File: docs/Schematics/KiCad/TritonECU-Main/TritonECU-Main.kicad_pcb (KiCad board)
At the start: 4 copper layers, 158 x 174 mm, 4 parts, among them J1 EEC-V 104

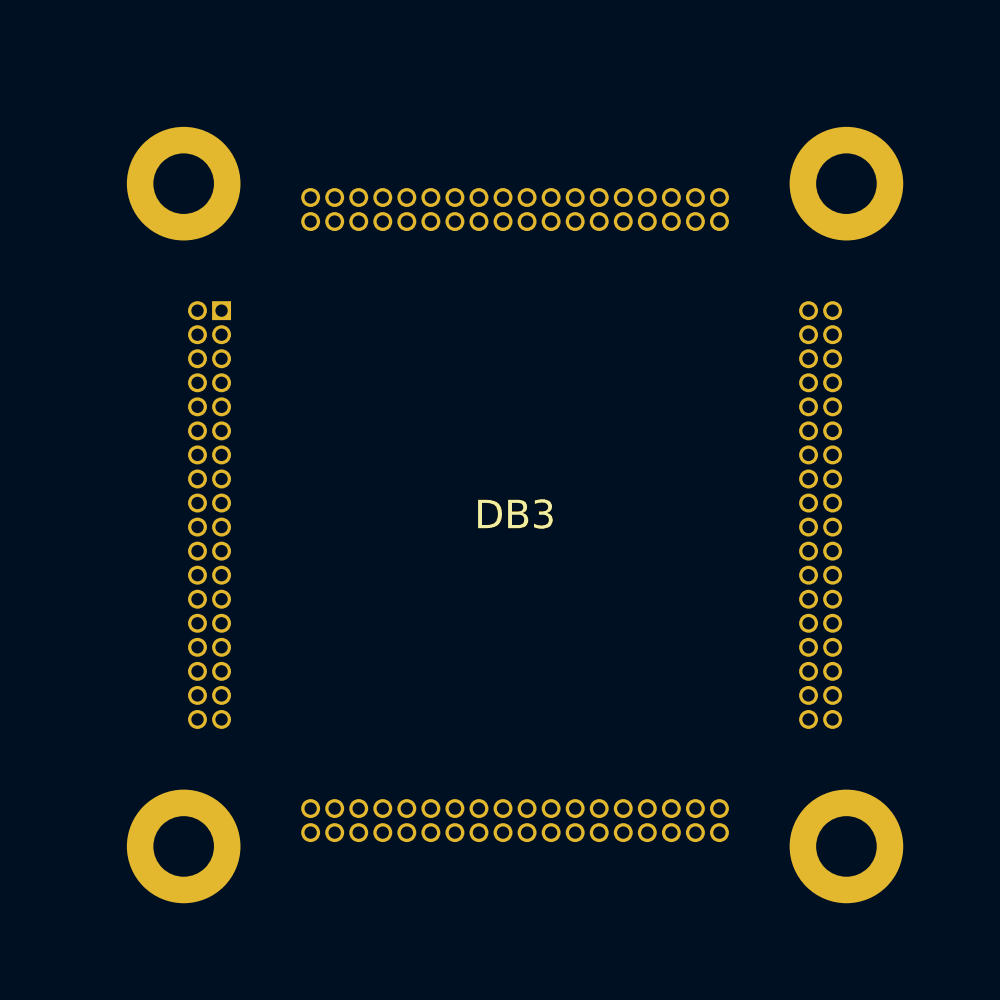
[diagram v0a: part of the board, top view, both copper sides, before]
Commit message: MCU module: place 6-layer PCB with Samtec SMT headers and STDC14
gen_module_pcb.py builds the 44 x 44 mm, 6-layer module board in KiCad's
Python. The stack is F sig / In1 GND / In2 sig / In3 sig / In4 +3.3V / B sig.
The F767 is on top; decoupling, crystals and the headers are on the bottom.

The headers are Samtec TFM-118-22-L-D-A (module bottom) and
SFM-118-02-S-D-A-N-K-TR (carrier top), both SMT. Pad geometry and alignment
holes come from the vendor footprints imported via Component Search Engine;
positions come from mcu_pinout.py, and the rows now sit at 16.5 mm so the TFM
bodies clear at the corners. The carrier DB3 footprint is regenerated to match,
and all 144 pins are verified to mate.

The H1 standoff is offset 0.7 mm per axis, so the module fits only one way
round: the no-notch socket and four identical headers give no polarization.

An STDC14 programming header (FTSH-107, SMT) on the module top carries SWD,
SWO, NRST and the ST-Link VCP on USART3 PD8/PD9. Passives use hand-solder
footprints.

Co-Authored-By: Claude Opus 5.5 <noreply@anthropic.com>
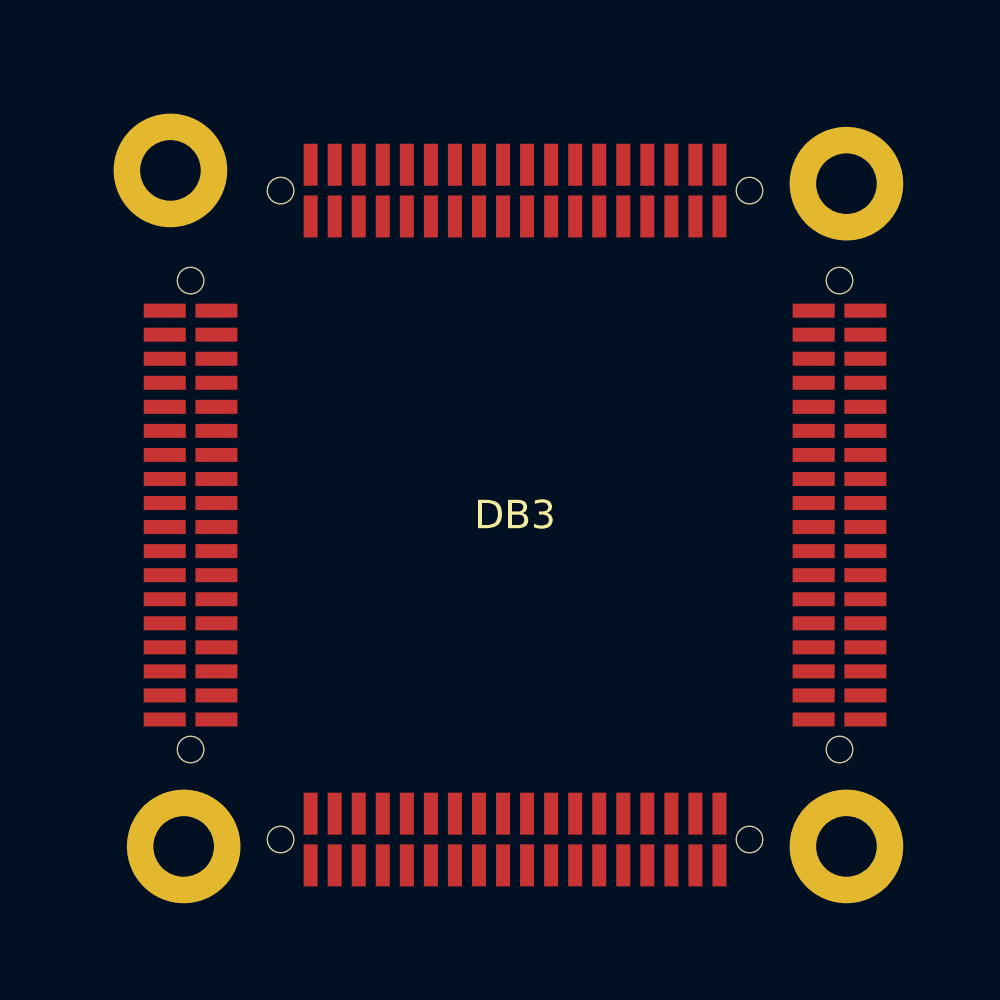
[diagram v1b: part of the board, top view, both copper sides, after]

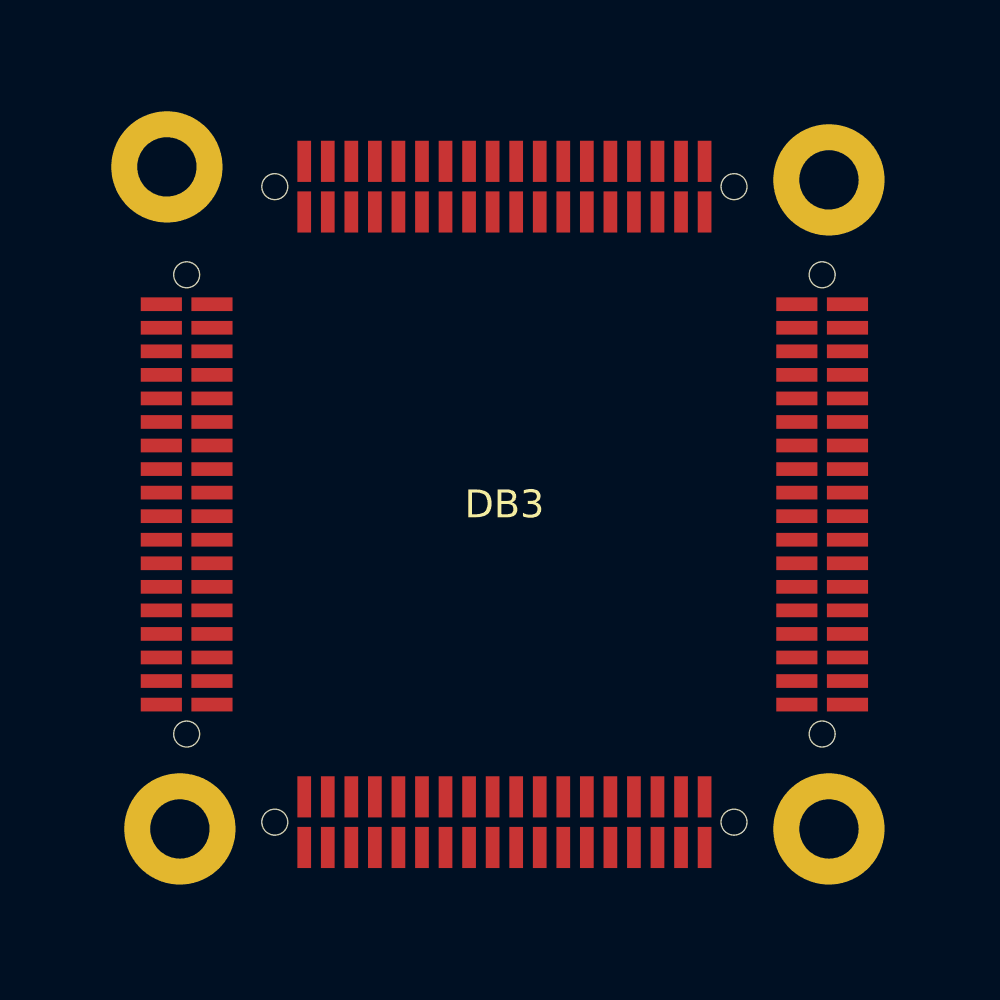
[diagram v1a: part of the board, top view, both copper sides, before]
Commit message: MCU module: route 46 mm board on Samtec FTSH/FLE with Wurth/PEM standoffs
- Interconnect: FTSH-118-02-L-DV-A (module bottom) mating FLE-118-01-G-DV-K-TR
  (carrier top), 7.47 mm stack, replacing TFM-118-22 / SFM-118-02. FTSH pads
  trimmed 0.1 mm at the inner end for the 0.25 mm hole clearance to the -A
  alignment holes.
- Standoffs: Wurth 9774050982R 5 mm SMT spacer on the module, PEM
  SMTSO-M3-2ET 2 mm on the carrier, 0.5 mm M3 washer between (7.5 mm),
  M3 x 10 screw. Spacer footprint generated from the Wurth land pattern with
  a GND ring, plus Wurth's STEP model.
- Module grows 44 -> 46 mm for the spacer pads; H1 keying offset now inward.
- Board routed with Freerouting: DRC 0 violations, 0 unconnected, schematic
  parity clean. All parts included in the BOM; supplier BOM exports added.
- Generators: fix footprint-to-symbol links (netlist tstamps regex), copy all
  schematic fields, skip no-connect pins, footprint-only mode in gen_module.py,
  carrier floor plan refreshes a changed mate footprint in place.

Co-Authored-By: Claude Opus 5.5 <noreply@anthropic.com>
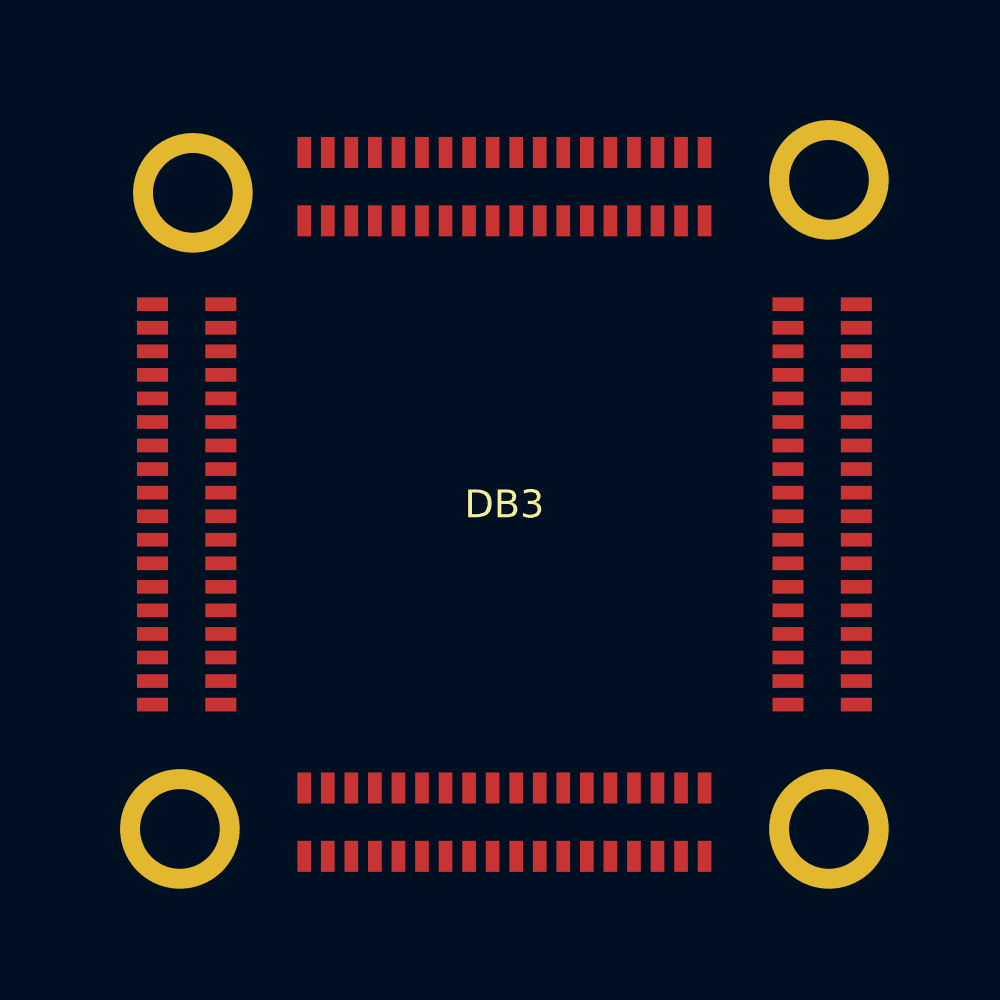
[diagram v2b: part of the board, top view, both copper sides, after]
